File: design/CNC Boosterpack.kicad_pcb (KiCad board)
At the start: 2 copper layers, 58.4 x 62.5 mm, 68 parts, among them J1 JP1, J10 EEPROMaddr, J11 UART/GPIO, J2 JP2, J3 JP3, J4 I2CDrv, J5 I2C, J6 RESET, J7 VDrvGND, J8 VDrvSel, J9 Spindle/Coolant, P1 CONN_02x10, P12 YA, P13 YB, P14 ZA, P15 ZB, P17 VMOT, P2 GPIO, P3 Control, P6 XB, P7 CONN_02x10, P8 Limits, P9 XA, Q1 2N7002, Q2 2N7002, Q3 2N7002, Q4 2N7002, U1 TLP290-4, U2 TLP290-4, U3 TLP290-4, U4 24LC16, U5 TCA9406

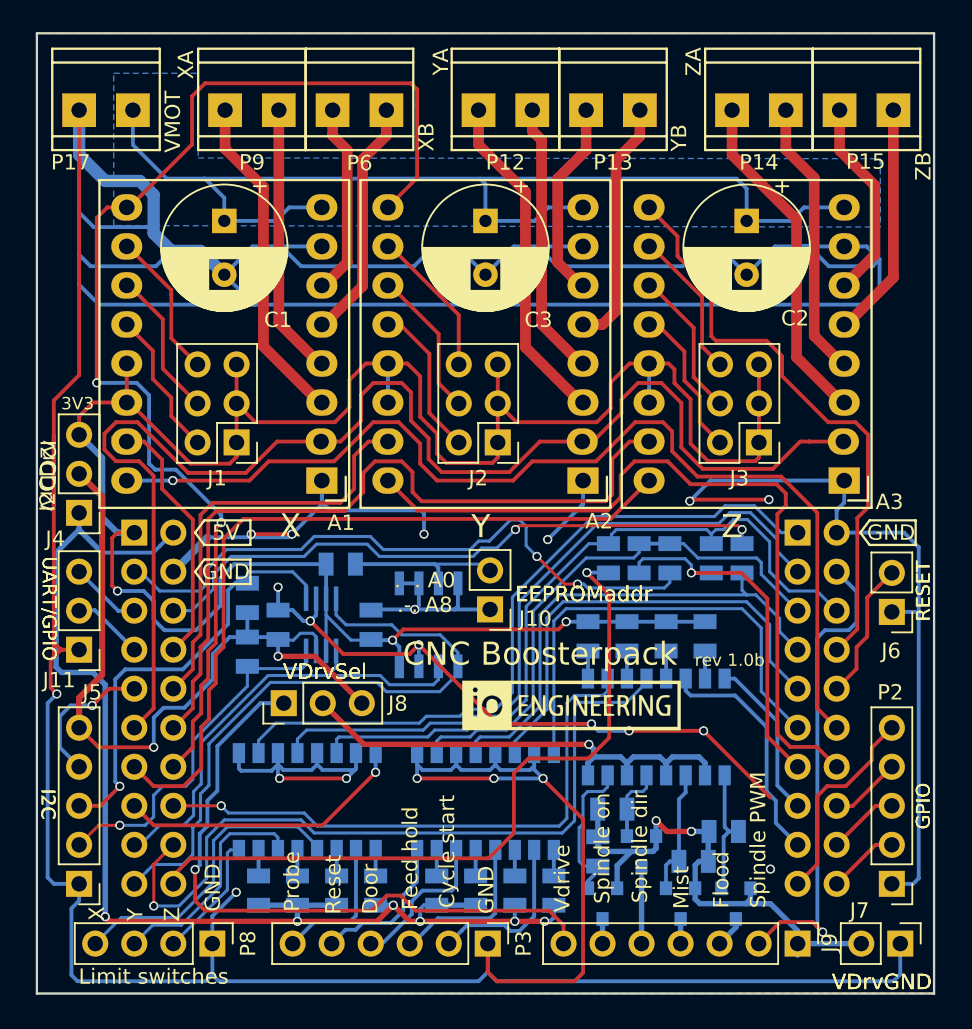
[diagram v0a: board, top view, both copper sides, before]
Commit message: Updated to latest revision
A small batch of the Trinamic-version PCB has been made, driver
development in good progress. Marlin-style M-commands will be supported
including status reports. Grbl protocol extensions allows real-trime
plotting of data (stallguard value) for simpler tuning.
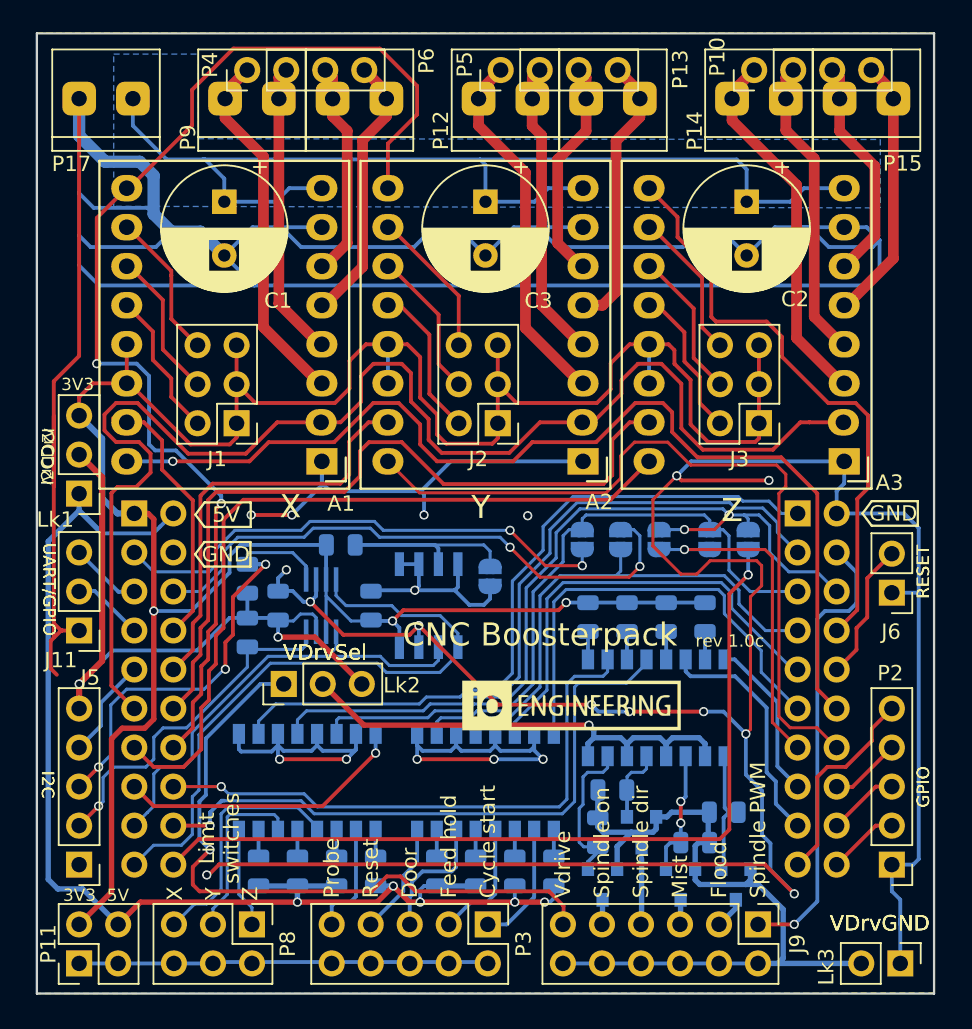
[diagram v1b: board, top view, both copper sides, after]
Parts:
- removed J7: VDrvGND, Connector_PinHeader_2.54mm:PinHeader_1x02_P2.54mm_Vertical
- added Lk3: VDrvGND, Connector_PinHeader_2.54mm:PinHeader_1x02_P2.54mm_Vertical, F.Cu at (56.2, -1.96)
- added P10: ZMotor, IoEngineering:PinHeader_1x04_P2.54mm_Vertical_Motor, F.Cu at (46.7, -60.1)
- added P11: Limits, Connector_PinHeader_2.54mm:PinHeader_2x02_P2.54mm_Vertical, F.Cu at (2.75, -1.96)
- added P4: XMotor, IoEngineering:PinHeader_1x04_P2.54mm_Vertical_Motor, F.Cu at (13.7, -60.1)
- added P5: YMotor, IoEngineering:PinHeader_1x04_P2.54mm_Vertical_Motor, F.Cu at (30.2, -60.1)
- J12: renamed from R14; value 0R -> 0; footprint Resistor_SMD:R_0805_2012Metric -> Jumper:SolderJumper-2_P1.3mm_Open_RoundedPad1.0x1.5mm
- J13: renamed from R10; value 0R -> 0; footprint Resistor_SMD:R_0805_2012Metric -> Jumper:SolderJumper-2_P1.3mm_Open_RoundedPad1.0x1.5mm
- J14: renamed from R11; value 0R -> 0; footprint Resistor_SMD:R_0805_2012Metric -> Jumper:SolderJumper-2_P1.3mm_Open_RoundedPad1.0x1.5mm
- J15: renamed from R13; value 0R -> 0; footprint Resistor_SMD:R_0805_2012Metric -> Jumper:SolderJumper-2_P1.3mm_Open_RoundedPad1.0x1.5mm
- J16: renamed from R12; value 0R -> 0; footprint Resistor_SMD:R_0805_2012Metric -> Jumper:SolderJumper-2_P1.3mm_Open_RoundedPad1.0x1.5mm
- J9: footprint Connector_PinHeader_2.54mm:PinHeader_1x07_P2.54mm_Vertical -> Connector_PinHeader_2.54mm:PinHeader_2x06_P2.54mm_Vertical
- Lk4: renamed from J10; footprint Connector_PinHeader_2.54mm:PinHeader_1x02_P2.54mm_Vertical -> Jumper:SolderJumper-2_P1.3mm_Open_RoundedPad1.0x1.5mm; moved to B.Cu
- P12, P13, P14, P15, P17, P6, P9: footprint IoEngineering:CONN_PWR_2P_3.5MM -> IoEngineering:CONN_PWR_2P_3.5MM_CAMBLOCK
- P3: footprint Connector_PinHeader_2.54mm:PinHeader_1x06_P2.54mm_Vertical -> Connector_PinHeader_2.54mm:PinHeader_2x05_P2.54mm_Vertical
- P8: footprint Connector_PinHeader_2.54mm:PinHeader_1x04_P2.54mm_Vertical -> Connector_PinHeader_2.54mm:PinHeader_2x03_P2.54mm_Vertical
- moved J13 9.18 mm to (46.3, -29.6), turned to 90 degrees
- moved J15 7.99 mm to (38.0, -29.6), turned to 270 degrees
- moved J16 5.83 mm to (35.5, -29.6), turned to 90 degrees
- moved J14 4.76 mm to (43.8, -29.6), turned to 90 degrees
- moved J12 3.61 mm to (40.5, -29.6), turned to 90 degrees
- moved J9 2.87 mm to (46.9, -4.50)
- moved P8 2.87 mm to (14.0, -4.50)
- moved Lk4 2.15 mm to (29.5, -27.1), turned to 90 degrees
- moved REF** 1.26 mm to (55.7, -31.2)
- moved J5 1.25 mm to (2.75, -8.39)
- moved P2 1.25 mm to (55.6, -8.39)
- moved A1 1.25 mm to (18.6, -34.6)
- moved A2 1.25 mm to (35.5, -34.6)
- moved A3 1.25 mm to (52.5, -34.6)
- moved C1 1.25 mm to (12.2, -51.5)
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- renumbered J4 to Lk1, J8 to Lk2
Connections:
- J12 pad 1: /PE0 -> /PC7
- J12 pad 2: /PC7 -> /PE0
- J13 pad 1: /PE0 -> /PF1
- J13 pad 2: /PF1 -> /PE0
- J14 pad 1: /PB3 -> /PC7
- J14 pad 2: /PC7 -> /PB3
- J15 pad 1: /PC4 -> /PD0
- J15 pad 2: /PD0 -> /PC4
- J16 pad 1: /PB3 -> /PB5
- J16 pad 2: /PB5 -> /PB3
- J9 pad 1: Net-(J7-Pad2) -> /PB2
- J9 pad 2: /PB2 -> Net-(J9-Pad10)
- J9 pad 4: Net-(J9-Pad4) -> Net-(J9-Pad10)
- J9 pad 6: Net-(J9-Pad6) -> Net-(J9-Pad10)
- J9 pad 7: Net-(J8-Pad1) -> Net-(J9-Pad7)
- Lk2 pad 1: Net-(J8-Pad1) -> Net-(J9-Pad11)
- P3 pad 1: GND -> /CS
- P3 pad 2: /CS -> GND
- P3 pad 4: /SD -> GND
- P3 pad 5: /Reset -> /SD
- P3 pad 6: /Probe -> GND
- P8 pad 1: GND -> /LimZ
- P8 pad 2: /LimZ -> GND
- P8 pad 4: /LimX -> GND
- Q1 pad 2: Net-(J7-Pad2) -> Net-(J9-Pad10)
- Q1 pad 3: Net-(J9-Pad6) -> Net-(J9-Pad9)
- Q2 pad 2: Net-(J7-Pad2) -> Net-(J9-Pad10)
- Q3 pad 2: Net-(J7-Pad2) -> Net-(J9-Pad10)
- Q3 pad 3: Net-(J9-Pad4) -> Net-(J9-Pad5)
- Q4 pad 2: Net-(J7-Pad2) -> Net-(J9-Pad10)
- Q4 pad 3: Net-(J9-Pad5) -> Net-(J9-Pad7)
- R18 pad 2: Net-(J7-Pad2) -> Net-(J9-Pad10)
- R19 pad 2: Net-(J7-Pad2) -> Net-(J9-Pad10)
- R20 pad 2: Net-(J7-Pad2) -> Net-(J9-Pad10)
- R21 pad 2: Net-(J7-Pad2) -> Net-(J9-Pad10)
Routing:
- net Net-(J9-Pad10): track 0.00 -> 49.5 mm
- net Net-(J9-Pad11): track 0.00 -> 43.7 mm, vias 0 -> 1
- net Net-(J8-Pad1): track 42.8 -> 0.00 mm, vias 1 -> 0
- net Net-(J7-Pad2): track 34.6 -> 0.00 mm, vias 2 -> 0
- net /3V3: track 155.6 -> 176.5 mm
- net GND: track 496.8 -> 487.2 mm
- net /PE3: track 49.5 -> 41.0 mm
- net /PB5: track 41.9 -> 33.8 mm
- net /PF1: track 47.9 -> 55.9 mm
- net /PE0: track 47.8 -> 52.9 mm, vias 0 -> 2
- net Net-(J9-Pad7): track 0.00 -> 5.00 mm
- net /PD0: track 41.6 -> 37.7 mm
- net /VCCB: track 49.5 -> 45.7 mm
- net /LimX: track 19.9 -> 16.1 mm
- net Net-(J9-Pad5): track 5.00 -> 1.60 mm
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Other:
- board text added: "5V"
- board text added: "MSP432 - Tiva -"
- board text added: "rev 1.0c"
- board text removed: "MSP432 Tiva"
- board text removed: "rev 1.0b"
